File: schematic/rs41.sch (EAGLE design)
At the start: 267 parts, among them J201 SENSORBOOM, Q201 BSS92, Q202 BSS92, Q203 BSS101, Q204 BSS101, Q501 BSS92, Q502 BSS101, Q503 BSS101, Q601 BSS101, U101 STM32F100C8LQFP48, U201 TS3A4751, U202 TS5A9411, U203 TS5A9411, U204 TS5A9411, U205 74HCU04, U206 305G, U207 74LVC3G34, U208 Z27F, U301 DIFFGEN, U302 UBX-6010MLF56, U303 SAW, U304 LNA, U401 SI4032QFN204X4, U501 TLV70030SOT23-5, U502 TPS61200, U503 TLV70030SOT23-5, U504 TLV70030SOT23-5, U601 25AA080SN, X101 OSC_MCU, X301 OSC_GPSXTAL4

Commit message: Fixed some errors on schematics.
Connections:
- net RADIO_UNKNOWN3 renamed RADIO_PROBE_POINT
- removed net ?: R206.2
- removed net GPS_UNKNOWN1: R309.1
- removed net N$29: R224.1, U201SPST1.NO, U201SPST2.NO, U201SPST3.NO, U201SPST4.NO, U207BUF1.Y
- removed net RADIO_UNKNOWN1: C401.2
- removed net RADIO_UNKNOWN2: R401.1
- new net GPS_CLK: C401.2, R309.1
- new net N$25: R208.2, U201SPST1.NO
- net +3V_ANA: now also R206.2
- net FRONTEND_UNKNOWN_1: now also C114.1, R106.1
- net FRONTEND_UNKNOWN_2: now also R125.1; no longer C114.1, R106.1
- net GND: now also R401.1
- net N$13: now also R224.1, U201SPST2.COM, U201SPST3.COM, U201SPST4.COM, U207BUF1.Y; no longer R208.2
- net N$130: no longer R125.1
- net N$26: now also U201SPST2.NO; no longer U201SPST2.COM
- net N$27: now also J201TMP.TEMP, U201SPST4.NO; no longer J201TMP.HYG_TEMP, U201SPST3.COM
- net N$28: now also J201TMP.HYG_TEMP, U201SPST3.NO; no longer J201TMP.TEMP, U201SPST4.COM
- net N$3: now also U208.IN1; no longer U208.IN3
- net N$4: now also U208.IN3; no longer U208.IN1
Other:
- moved on the sheet: C116, C220, C221, C302, C303, C304, C305, C402, C403, C404, C406, C407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

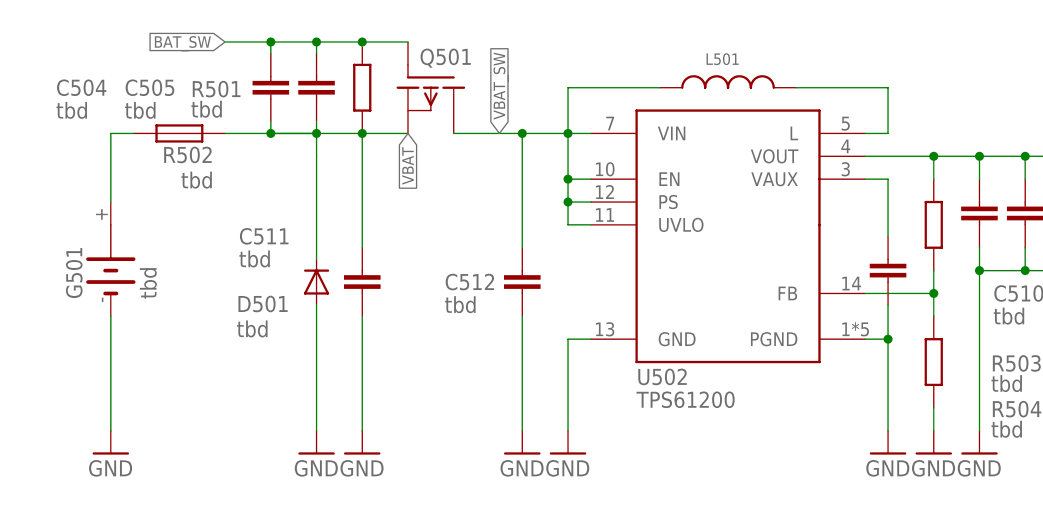
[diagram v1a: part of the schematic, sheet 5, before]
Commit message: added easaly readable values, used new symbols
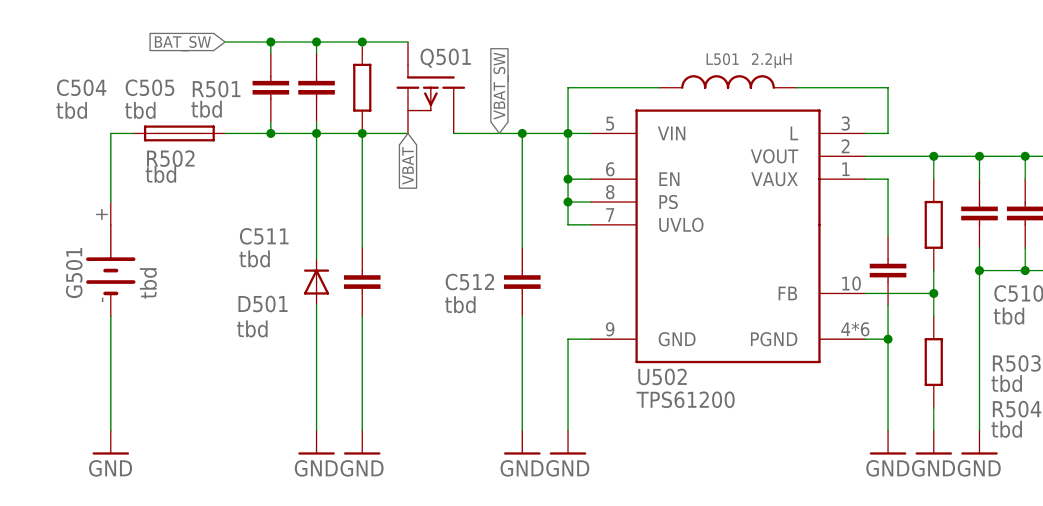
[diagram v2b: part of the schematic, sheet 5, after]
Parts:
- L501: value (none) -> 2.2µH
- R502: device rcl:R-EU_R0402 -> rs41:FUSE
- X101: value OSC_MCU -> 24MHz
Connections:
- net N$35: now also R502.1; no longer R502.2
- net VBAT: now also R502.2; no longer R502.1
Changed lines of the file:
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@@
 <part name="C520" library="rcl" library_urn="urn:adsk.eagle:library:334" deviceset="C-EU" device="C0402" package3d_urn="urn:adsk.eagle:package:23626/1" value="tbd"/>
 <part name="GND519" library="supply1" library_urn="urn:adsk.eagle:library:371" deviceset="GND" device=""/>
-<part name="L501" library="PowerMagnetics (rev17e)" deviceset="WE-MAPI_3020" device="" technology="_74438336100"/>
+<part name="L501" library="PowerMagnetics (rev17e)" deviceset="WE-MAPI_3020" device="" technology="_74438336100" value="2.2µH"/>
 <part name="C512" library="rcl" library_urn="urn:adsk.eagle:library:334" deviceset="C-EU" device="C0402" package3d_urn="urn:adsk.eagle:package:23626/1" value="tbd"/>
 <part name="C510" library="rcl" library_urn="urn:adsk.eagle:library:334" deviceset="C-EU" device="C0402" package3d_urn="urn:adsk.eagle:package:23626/1" value="tbd"/>
@@
 <part name="GND511" library="supply1" library_urn="urn:adsk.eagle:library:371" deviceset="GND" device=""/>
 <part name="GND510" library="supply1" library_urn="urn:adsk.eagle:library:371" deviceset="GND" device=""/>
-<part name="R502" library="rcl" library_urn="urn:adsk.eagle:library:334" deviceset="R-EU_" device="R0402" package3d_urn="urn:adsk.eagle:package:23547/2" value="tbd"/>
 <part name="G501" library="battery" library_urn="urn:adsk.eagle:library:109" deviceset="2V60R" device="" package3d_urn="urn:adsk.eagle:package:4596/1" value="tbd"/>
 <part name="GND509" library="supply1" library_urn="urn:adsk.eagle:library:371" deviceset="GND" device=""/>
@@
 <part name="C110" library="rcl" library_urn="urn:adsk.eagle:library:334" deviceset="C-EU" device="C0402" package3d_urn="urn:adsk.eagle:package:23626/1" value="tbd"/>
 <part name="C111" library="rcl" library_urn="urn:adsk.eagle:library:334" deviceset="C-EU" device="C0402" package3d_urn="urn:adsk.eagle:package:23626/1" value="tbd"/>
-<part name="X101" library="rs41" deviceset="OSC_MCU" device="" package3d_urn="urn:adsk.eagle:package:7070708/1"/>
+<part name="X101" library="rs41" deviceset="OSC_MCU" device="" package3d_urn="urn:adsk.eagle:package:7070708/1" value="24MHz"/>
 <part name="C112" library="rcl" library_urn="urn:adsk.eagle:library:334" deviceset="C-EU" device="C0402" package3d_urn="urn:adsk.eagle:package:23626/1" value="tbd"/>
 <part name="R101" library="rcl" library_urn="urn:adsk.eagle:library:334" deviceset="R-EU_" device="R0402" package3d_urn="urn:adsk.eagle:package:23547/2" value="tbd"/>
@@
 <part name="P+2" library="rs41" deviceset="+3V_ANA" device=""/>
 <part name="GND5" library="supply1" library_urn="urn:adsk.eagle:library:371" deviceset="GND" device=""/>
+<part name="R502" library="rs41" deviceset="FUSE" device="" value="tbd"/>
 </parts>
 <sheets>
@@
 </instance>
 <instance part="X101" gate="G$1" x="-7.62" y="81.28" smashed="yes">
-<attribute name="NAME" x="-16.51" y="81.28" size="1.778" layer="95"/>
-<attribute name="VALUE" x="-22.86" y="78.74" size="1.778" layer="96"/>
+<attribute name="NAME" x="-20.32" y="81.28" size="1.778" layer="95"/>
+<attribute name="VALUE" x="-20.32" y="78.74" size="1.778" layer="96"/>
 </instance>
 <instance part="C112" gate="G$1" x="-2.54" y="68.58" smashed="yes" rot="R90">
@@
 <description>PSU</description>
 <plain>
-<wire x1="-25.4" y1="48.26" x2="-20.32" y2="48.26" width="0.1524" layer="94"/>
 <wire x1="182.88" y1="63.5" x2="96.52" y2="63.5" width="0.508" layer="98"/>
 <wire x1="96.52" y1="63.5" x2="-45.72" y2="63.5" width="0.508" layer="98"/>
@@
 <instance part="L501" gate="G$1" x="38.1" y="53.34" smashed="yes">
 <attribute name="NAME" x="35.56" y="55.88" size="1.27" layer="95"/>
-<attribute name="VALUE" x="35.56" y="50.8" size="1.27" layer="96"/>
+<attribute name="VALUE" x="40.64" y="55.88" size="1.27" layer="96"/>
 </instance>
 <instance part="C512" gate="G$1" x="15.24" y="33.02" smashed="yes">
@@
 <attribute name="VALUE" x="-10.16" y="10.16" size="1.778" layer="96"/>
 </instance>
-<instance part="R502" gate="G$1" x="-22.86" y="48.26" smashed="yes" rot="R180">
-<attribute name="NAME" x="-19.05" y="46.7614" size="1.778" layer="95" rot="R180"/>
-<attribute name="VALUE" x="-19.05" y="43.942" size="1.778" layer="96" rot="R180"/>
-</instance>
 <instance part="G501" gate="1" x="-30.48" y="33.02" smashed="yes" rot="R90">
 <attribute name="NAME" x="-33.655" y="29.845" size="1.778" layer="95" rot="R90"/>
@@
 <attribute name="VALUE" x="63.5" y="-27.94" size="1.778" layer="96"/>
 </instance>
+<instance part="R502" gate="F1" x="-22.86" y="48.26" smashed="yes">
+<attribute name="NAME" x="-26.67" y="44.577" size="1.778" layer="95"/>
+<attribute name="VALUE" x="-26.67" y="42.799" size="1.778" layer="96"/>
+</instance>
 </instances>
 <busses>
@@
 <pinref part="C504" gate="G$1" pin="2"/>
 <wire x1="-2.54" y1="48.26" x2="-7.62" y2="48.26" width="0.1524" layer="91"/>
-<wire x1="-7.62" y1="48.26" x2="-12.7" y2="48.26" width="0.1524" layer="91"/>
 <wire x1="-12.7" y1="49.53" x2="-12.7" y2="48.26" width="0.1524" layer="91"/>
 <wire x1="-12.7" y1="48.26" x2="-7.62" y2="48.26" width="0.1524" layer="91"/>
@@
 <wire x1="-2.54" y1="48.26" x2="-2.54" y2="35.56" width="0.1524" layer="91"/>
 <junction x="-2.54" y="48.26"/>
-<wire x1="-7.62" y1="45.72" x2="-7.62" y2="48.26" width="0.1524" layer="91"/>
-<pinref part="R502" gate="G$1" pin="1"/>
 <wire x1="-17.78" y1="48.26" x2="-12.7" y2="48.26" width="0.1524" layer="91"/>
 <junction x="-12.7" y="48.26"/>
 <pinref part="D501" gate="1" pin="C"/>
-<wire x1="-7.62" y1="34.29" x2="-7.62" y2="45.72" width="0.1524" layer="91"/>
+<wire x1="-7.62" y1="34.29" x2="-7.62" y2="48.26" width="0.1524" layer="91"/>
 <label x="2.54" y="48.26" size="1.27" layer="95" rot="R270" xref="yes"/>
 <pinref part="R501" gate="G$1" pin="1"/>
+<pinref part="R502" gate="F1" pin="2"/>
 </segment>
 <segment>
@@
 <segment>
 <pinref part="G501" gate="1" pin="+"/>
-<pinref part="R502" gate="G$1" pin="2"/>
 <wire x1="-30.48" y1="40.64" x2="-30.48" y2="48.26" width="0.1524" layer="91"/>
 <wire x1="-30.48" y1="48.26" x2="-27.94" y2="48.26" width="0.1524" layer="91"/>
+<pinref part="R502" gate="F1" pin="1"/>
 </segment>
 </net>

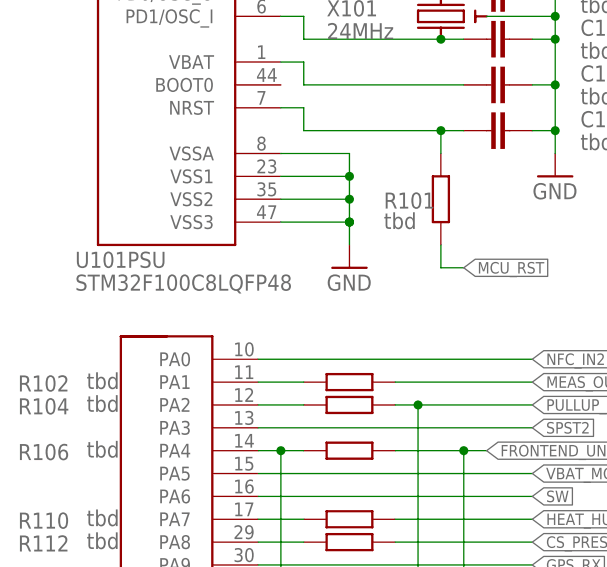
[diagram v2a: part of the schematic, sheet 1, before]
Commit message: changed MCU Value to match Part Print / ST Number
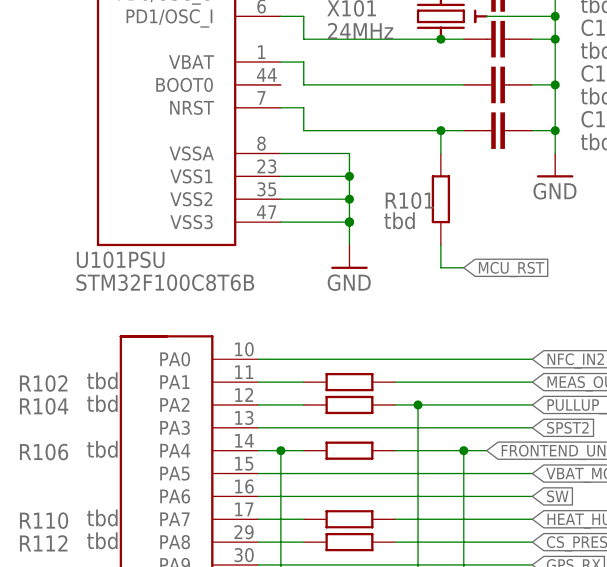
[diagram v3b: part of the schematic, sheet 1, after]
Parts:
- U101: value STM32F100C8LQFP48 -> STM32F100C8T6B
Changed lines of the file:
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@@
 </classes>
 <parts>
-<part name="U101" library="rs41" deviceset="STM32F100C8" device="LQFP48" package3d_urn="urn:adsk.eagle:package:19290/1"/>
+<part name="U101" library="rs41" deviceset="STM32F100C8" device="LQFP48" package3d_urn="urn:adsk.eagle:package:19290/1" value="STM32F100C8T6B"/>
 <part name="U302" library="rs41" deviceset="UBX-6010" device="MLF56" package3d_urn="urn:adsk.eagle:package:7034635/1"/>
 <part name="U401" library="rs41" deviceset="SI4032" device="QFN204X4" package3d_urn="urn:adsk.eagle:package:7012035/1"/>

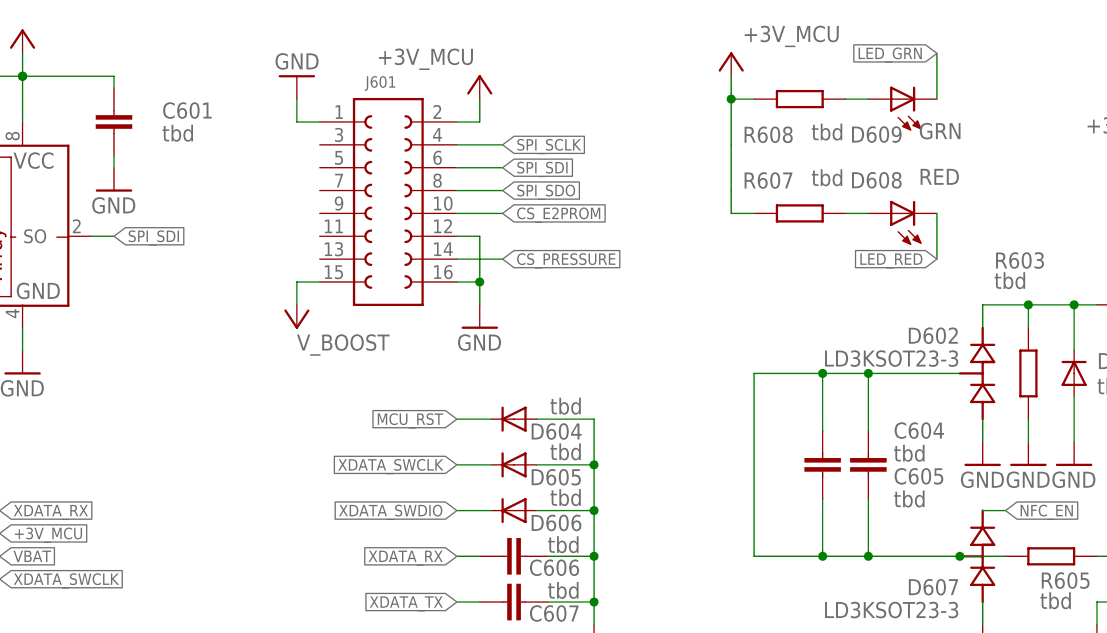
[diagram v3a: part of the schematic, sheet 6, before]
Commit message: replaced tbd with DNP for unpopulated components
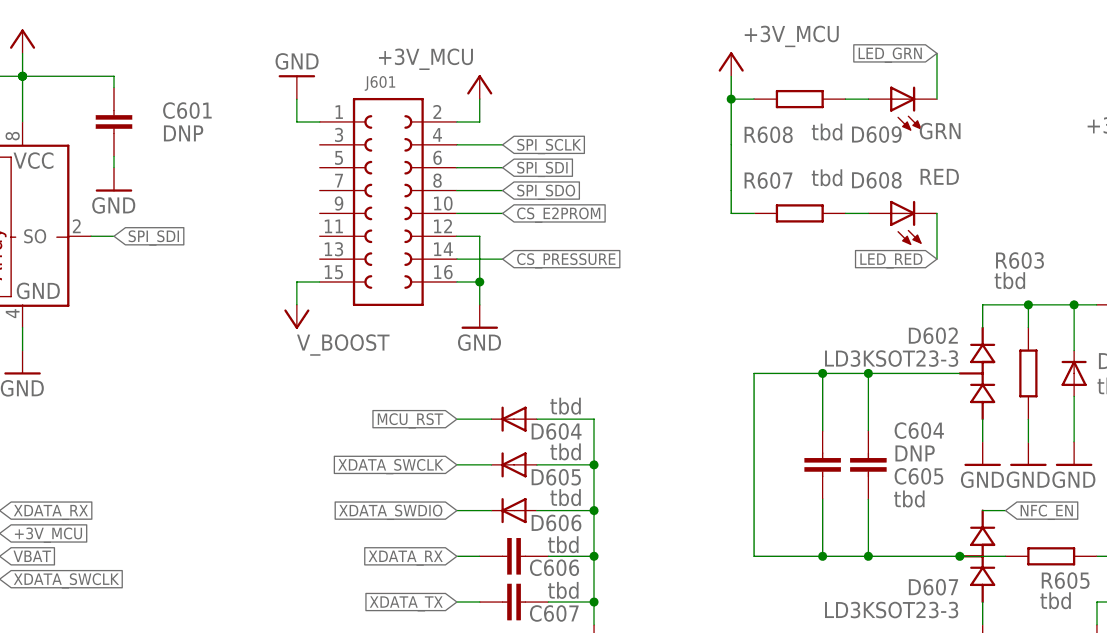
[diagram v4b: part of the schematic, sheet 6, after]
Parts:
- C601, C604, R124: value tbd -> DNP
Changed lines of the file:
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@@
 <part name="GND112" library="supply1" library_urn="urn:adsk.eagle:library:371" deviceset="GND" device=""/>
 <part name="GND111" library="supply1" library_urn="urn:adsk.eagle:library:371" deviceset="GND" device=""/>
-<part name="R124" library="rcl" library_urn="urn:adsk.eagle:library:334" deviceset="R-EU_" device="R0402" package3d_urn="urn:adsk.eagle:package:23547/2" value="tbd"/>
+<part name="R124" library="rcl" library_urn="urn:adsk.eagle:library:334" deviceset="R-EU_" device="R0402" package3d_urn="urn:adsk.eagle:package:23547/2" value="DNP"/>
 <part name="GND110" library="supply1" library_urn="urn:adsk.eagle:library:371" deviceset="GND" device=""/>
 <part name="R125" library="rcl" library_urn="urn:adsk.eagle:library:334" deviceset="R-EU_" device="R0402" package3d_urn="urn:adsk.eagle:package:23547/2" value="tbd"/>
@@
 <part name="GND601" library="supply1" library_urn="urn:adsk.eagle:library:371" deviceset="GND" device=""/>
 <part name="GND603" library="supply1" library_urn="urn:adsk.eagle:library:371" deviceset="GND" device=""/>
-<part name="C601" library="rcl" library_urn="urn:adsk.eagle:library:334" deviceset="C-EU" device="C0402" package3d_urn="urn:adsk.eagle:package:23626/1" value="tbd"/>
+<part name="C601" library="rcl" library_urn="urn:adsk.eagle:library:334" deviceset="C-EU" device="C0402" package3d_urn="urn:adsk.eagle:package:23626/1" value="DNP"/>
 <part name="GND602" library="supply1" library_urn="urn:adsk.eagle:library:371" deviceset="GND" device=""/>
 <part name="GND604" library="supply1" library_urn="urn:adsk.eagle:library:371" deviceset="GND" device=""/>
@@
 <part name="R606" library="rcl" library_urn="urn:adsk.eagle:library:334" deviceset="R-EU_" device="R0402" package3d_urn="urn:adsk.eagle:package:23547/2" value="tbd"/>
 <part name="GND612" library="supply1" library_urn="urn:adsk.eagle:library:371" deviceset="GND" device=""/>
-<part name="C604" library="rcl" library_urn="urn:adsk.eagle:library:334" deviceset="C-EU" device="C0402" package3d_urn="urn:adsk.eagle:package:23626/1" value="tbd"/>
+<part name="C604" library="rcl" library_urn="urn:adsk.eagle:library:334" deviceset="C-EU" device="C0402" package3d_urn="urn:adsk.eagle:package:23626/1" value="DNP"/>
 <part name="R607" library="rcl" library_urn="urn:adsk.eagle:library:334" deviceset="R-EU_" device="R0402" package3d_urn="urn:adsk.eagle:package:23547/2" value="tbd"/>
 <part name="R608" library="rcl" library_urn="urn:adsk.eagle:library:334" deviceset="R-EU_" device="R0402" package3d_urn="urn:adsk.eagle:package:23547/2" value="tbd"/>

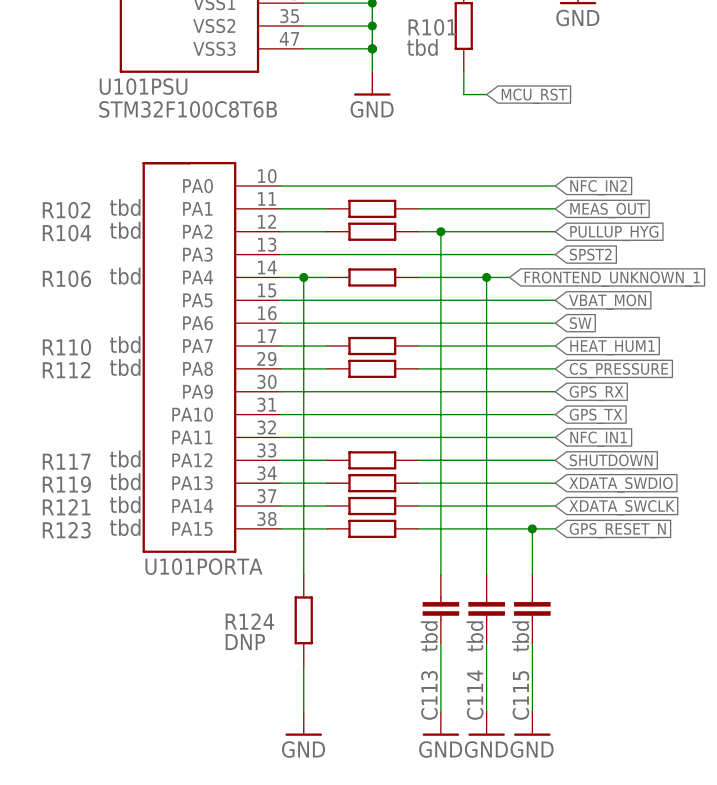
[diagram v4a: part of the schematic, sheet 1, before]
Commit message: fixed R124 beeing on the wrong side of R104
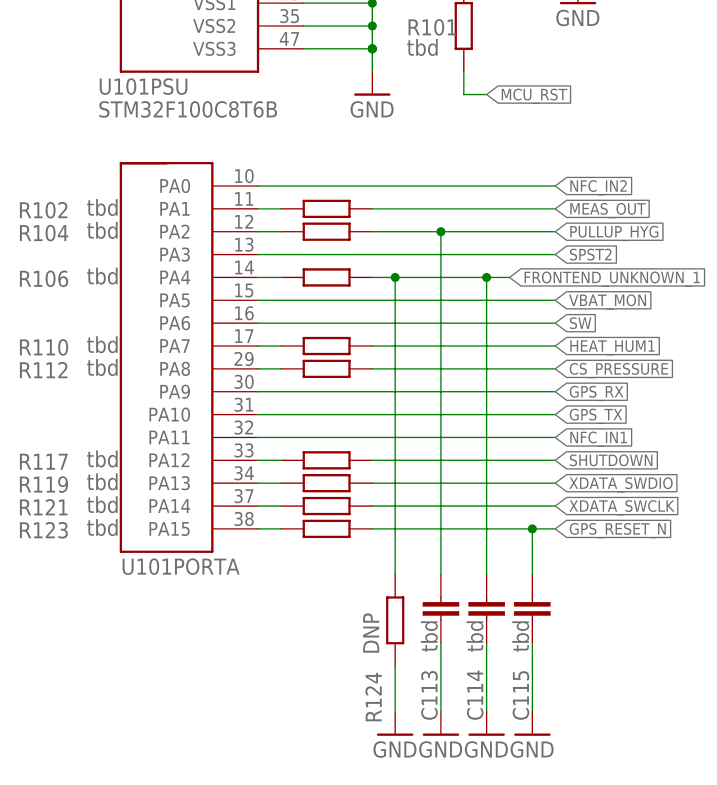
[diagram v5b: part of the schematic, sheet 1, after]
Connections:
- net FRONTEND_UNKNOWN_1: now also R124.1
- net N$98: no longer R124.1
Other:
- moved on the sheet: R102, R104, R106, R110, R112, R117, R119, R121, R123, R124, U101PORTA
